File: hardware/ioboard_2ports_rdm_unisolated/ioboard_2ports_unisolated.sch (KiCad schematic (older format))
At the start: 27 parts, among them J1 Conn_02x06_Odd_Even, J12 Conn_01x03, J2 XLR3, J3 XLR3, J6 Conn_01x03, J8 XLR3, J9 XLR3, U1 M24C02-WMN, U2 SP3485EN, U3 XC6206PxxxMR, U4 SP3485EN

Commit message: Unify board naming and bump all to rev 0.2
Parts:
- U3: LCSC (none) -> C5446
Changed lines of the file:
@@
 Title "rp2040_dongle_ioboard_2ports_rdm_unisolated"
 Date "2021-03-28"
-Rev "0.1"
+Rev "0.2"
 Comp "https://www.openlighting.org"
 Comment1 ""
@@
 F 2 "Package_TO_SOT_SMD:SOT-23" H 6750 1375 50  0001 C CIN
 F 3 "https://www.torexsemi.com/file/xc6206/XC6206.pdf" H 6750 1150 50  0001 C CNN
+F 4 "C5446" H 6750 1150 50  0001 C CNN "LCSC"
 	1    6750 1150
 	1    0    0    -1

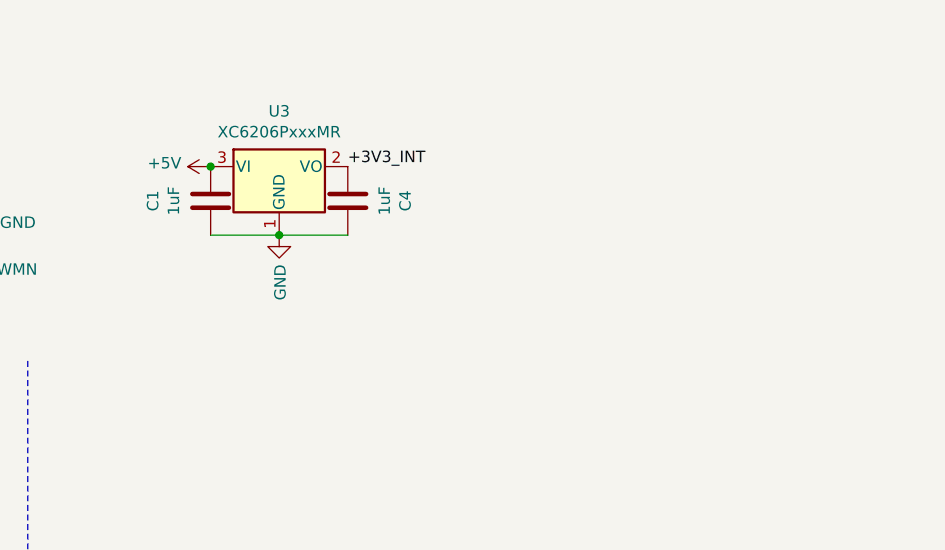
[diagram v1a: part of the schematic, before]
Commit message: ioboard_2ports_rdm_unisolated: Use AMS1117 LDO instead of the more exotic XC6206. Bump to Rev 0.3
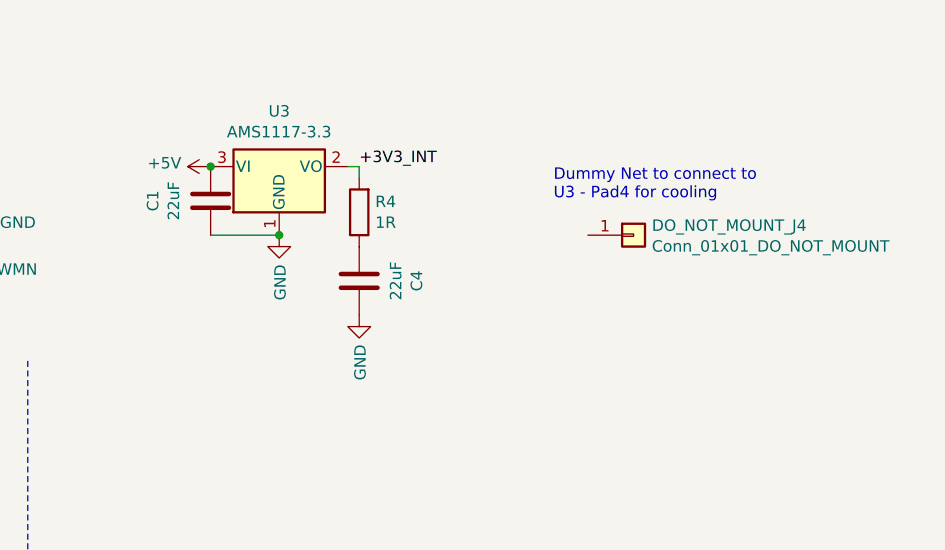
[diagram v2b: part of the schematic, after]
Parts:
- removed U3: XC6206PxxxMR, Package_TO_SOT_SMD:SOT-23, symbol Regulator_Linear:XC6206PxxxMR
- added DO_NOT_MOUNT_J4: Conn_01x01_DO_NOT_MOUNT, Connector_PinHeader_1.00mm:PinHeader_1x02_P1.00mm_Vertical_SMD_Pin1Left, symbol Connector_Generic:Conn_01x01
- added R4: 1R, Resistor_SMD:R_0805_2012Metric, symbol Device:R
- added U3: AMS1117-3.3, Package_TO_SOT_SMD:SOT-223, symbol Regulator_Linear:AMS1117-3.3
- C1, C4: value 1uF -> 22uF; footprint Capacitor_SMD:C_0603_1608Metric -> Capacitor_SMD:C_0805_2012Metric; LCSC C15849 -> C45783
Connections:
- net +3V3_INT: now also R4.2, U3.2 (VO); no longer C4.2
- net +5V: now also U3.3 (VI)
- net GND: now also U3.1 (GND)
- new net: C4.2, R4.1
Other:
- note added: "Dummy Net to connect to\nU3 - Pad4 for cooling"
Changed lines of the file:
@@
 Sheet 1 1
 Title "rp2040_dongle_ioboard_2ports_rdm_unisolated"
-Date "2021-03-28"
-Rev "0.2"
+Date "2021-04-06"
+Rev "0.3"
 Comp "https://www.openlighting.org"
 Comment1 ""
@@
 $EndComp
 $Comp
-L Regulator_Linear:XC6206PxxxMR U3
-U 1 1 606AA3C4
-P 6750 1150
-F 0 "U3" H 6750 1392 50  0000 C CNN
-F 1 "XC6206PxxxMR" H 6750 1301 50  0000 C CNN
-F 2 "Package_TO_SOT_SMD:SOT-23" H 6750 1375 50  0001 C CIN
-F 3 "https://www.torexsemi.com/file/xc6206/XC6206.pdf" H 6750 1150 50  0001 C CNN
-F 4 "C5446" H 6750 1150 50  0001 C CNN "LCSC"
-	1    6750 1150
-	1    0    0    -1
-$EndComp
-$Comp
 L power:+5V #PWR012
 U 1 1 606AD98F
@@
 P 6450 1300
 F 0 "C1" V 6198 1300 50  0000 C CNN
-F 1 "1uF" V 6289 1300 50  0000 C CNN
-F 2 "Capacitor_SMD:C_0603_1608Metric" H 6488 1150 50  0001 C CNN
+F 1 "22uF" V 6289 1300 50  0000 C CNN
+F 2 "Capacitor_SMD:C_0805_2012Metric" H 6488 1150 50  0001 C CNN
 F 3 "~" H 6450 1300 50  0001 C CNN
-F 4 "C15849" V 6450 1300 50  0001 C CNN "LCSC"
+F 4 "C45783" V 6450 1300 50  0001 C CNN "LCSC"
 	1    6450 1300
 	1    0    0    -1
 $EndComp
-Connection ~ 6450 1150
 $Comp
 L power:GND #PWR013
@@
 	6750 1450 6450 1450
 Connection ~ 6750 1450
-$Comp
-L Device:C C4
-U 1 1 606B6E82
-P 7050 1300
-F 0 "C4" V 6798 1300 50  0000 C CNN
-F 1 "1uF" V 6889 1300 50  0000 C CNN
-F 2 "Capacitor_SMD:C_0603_1608Metric" H 7088 1150 50  0001 C CNN
-F 3 "~" H 7050 1300 50  0001 C CNN
-F 4 "C15849" V 7050 1300 50  0001 C CNN "LCSC"
-	1    7050 1300
-	-1   0    0    1
-$EndComp
-Wire Wire Line
-	6750 1450 7050 1450
-Text Label 7050 1150 0    50   ~ 0
+Text Label 7100 1150 0    50   ~ 0
 +3V3_INT
 Text Label 1700 2800 0    50   ~ 0
@@
 Text Label 1950 5050 0    50   ~ 0
 +3V3_INT
+$Comp
+L Regulator_Linear:AMS1117-3.3 U3
+U 1 1 606CF145
+P 6750 1150
+F 0 "U3" H 6750 1392 50  0000 C CNN
+F 1 "AMS1117-3.3" H 6750 1301 50  0000 C CNN
+F 2 "Package_TO_SOT_SMD:SOT-223" H 6750 1350 50  0001 C CNN
+F 3 "http://www.advanced-monolithic.com/pdf/ds1117.pdf" H 6850 900 50  0001 C CNN
+F 4 "C6186" H 6750 1150 50  0001 C CNN "LCSC"
+	1    6750 1150
+	1    0    0    -1
+$EndComp
+Connection ~ 6450 1150
+$Comp
+L Device:C C4
+U 1 1 606D62FA
+P 7100 1650
+F 0 "C4" V 6848 1650 50  0000 C CNN
+F 1 "22uF" V 6939 1650 50  0000 C CNN
+F 2 "Capacitor_SMD:C_0805_2012Metric" H 7138 1500 50  0001 C CNN
+F 3 "~" H 7100 1650 50  0001 C CNN
+F 4 "C45783" V 7100 1650 50  0001 C CNN "LCSC"
+	1    7100 1650
+	-1   0    0    1
+$EndComp
+$Comp
+L Device:R R4
+U 1 1 606D850F
+P 7100 1350
+F 0 "R4" H 7030 1304 50  0000 R CNN
+F 1 "1R" H 7030 1395 50  0000 R CNN
+F 2 "Resistor_SMD:R_0805_2012Metric" V 7030 1350 50  0001 C CNN
+F 3 "~" H 7100 1350 50  0001 C CNN
+F 4 "C25271" H 7100 1350 50  0001 C CNN "LCSC"
+	1    7100 1350
+	-1   0    0    1
+$EndComp
+Wire Wire Line
+	7050 1150 7100 1150
+Wire Wire Line
+	7100 1150 7100 1200
+$Comp
+L power:GND #PWR014
+U 1 1 606DD4A5
+P 7100 1800
+F 0 "#PWR014" H 7100 1550 50  0001 C CNN
+F 1 "GND" V 7105 1672 50  0000 R CNN
+F 2 "" H 7100 1800 50  0001 C CNN
+F 3 "" H 7100 1800 50  0001 C CNN
+	1    7100 1800
+	1    0    0    -1
+$EndComp
+Text Notes 7950 1300 0    50   ~ 0
+Dummy Net to connect to\nU3 - Pad4 for cooling
+$Comp
+L Connector_Generic:Conn_01x01 DO_NOT_MOUNT_J4
+U 1 1 606ED99D
+P 8300 1450
+F 0 "DO_NOT_MOUNT_J4" H 8380 1492 50  0000 L CNN
+F 1 "Conn_01x01_DO_NOT_MOUNT" H 8380 1401 50  0000 L CNN
+F 2 "Connector_PinHeader_1.00mm:PinHeader_1x02_P1.00mm_Vertical_SMD_Pin1Left" H 8300 1450 50  0001 C CNN
+F 3 "~" H 8300 1450 50  0001 C CNN
+	1    8300 1450
+	1    0    0    -1
+$EndComp
 $EndSCHEMATC
